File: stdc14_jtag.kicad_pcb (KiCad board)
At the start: 2 copper layers, 38 x 29 mm, 7 parts, among them J1 STDC14, J2 JTAG14, J3 UART, J4 POWER, SW1 RST

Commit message: fix: solve bottom silkscreen legend errors
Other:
- board text added: "CLK"
- board text added: "IO/MS"
- board text removed: "SWCLK/TCK"
- board text removed: "SWDIO/TMS"
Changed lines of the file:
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@@
       ) (layer "B.SilkS") (width 0.01) (fill solid))
   )
-  (gr_line (start -403 83.82) (end -403 87.376) (layer "B.SilkS") (width 0.15))
-  (gr_line (start -403 76.708) (end -403.75 76.708) (layer "B.SilkS") (width 0.15))
-  (gr_line (start -403 80.2) (end -403 76.708) (layer "B.SilkS") (width 0.15))
-  (gr_line (start -403 87.376) (end -403.75 87.376) (layer "B.SilkS") (width 0.15))
+  (gr_line (start -415.036 86.36) (end -415.036 82.042) (layer "B.SilkS") (width 0.15))
+  (gr_line (start -415.798 92.202) (end -414.274 92.202) (layer "B.SilkS") (width 0.15))
+  (gr_line (start -415.036 88.392) (end -415.036 92.202) (layer "B.SilkS") (width 0.15))
+  (gr_line (start -415.798 82.042) (end -414.274 82.042) (layer "B.SilkS") (width 0.15))
   (gr_line (start -402 95) (end -402 74) (layer "Edge.Cuts") (width 0.1))
   (gr_arc (start -436 99) (mid -438.828427 97.828427) (end -440 95) (layer "Edge.Cuts") (width 0.1))
@@
   (gr_line (start -406 70) (end -436 70) (layer "Edge.Cuts") (width 0.1))
   (gr_arc (start -402 95) (mid -403.171573 97.828427) (end -406 99) (layer "Edge.Cuts") (width 0.1))
-  (gr_text "GND" (at -403 82 90) (layer "B.SilkS")
+  (gr_text "GND" (at -415.036 87.376) (layer "B.SilkS")
+    (effects (font (size 1 1) (thickness 0.15)) (justify mirror))
+  )
+  (gr_text "RST" (at -415.036 79.502) (layer "B.SilkS")
     (effects (font (size 1 1) (thickness 0.15)) (justify mirror))
   )
@@
     (effects (font (size 1.5 1.5) (thickness 0.3)) (justify right mirror))
   )
-  (gr_text "SWCLK/TCK" (at -409 87.2) (layer "B.SilkS")
+  (gr_text "CLK" (at -409.448 82.042) (layer "B.SilkS")
     (effects (font (size 1 1) (thickness 0.15)) (justify left mirror))
   )
-  (gr_text "JTDI" (at -409 82.12) (layer "B.SilkS")
+  (gr_text "JTDI" (at -409.448 87.122) (layer "B.SilkS")
     (effects (font (size 1 1) (thickness 0.15)) (justify left mirror))
   )
@@
     (effects (font (size 1.5 1.5) (thickness 0.3)) (justify right mirror))
   )
-  (gr_text "VCC" (at -409 92.28) (layer "B.SilkS")
+  (gr_text "VCC" (at -409.448 76.962) (layer "B.SilkS")
     (effects (font (size 1 1) (thickness 0.15)) (justify left mirror))
   )
-  (gr_text "NC" (at -409 79.58) (layer "B.SilkS")
-    (effects (font (size 1 1) (thickness 0.15)) (justify left mirror))
-  )
-  (gr_text "RST" (at -403 89.25 90) (layer "B.SilkS")
-    (effects (font (size 1 1) (thickness 0.15)) (justify mirror))
+  (gr_text "NC" (at -411.734 89.662) (layer "B.SilkS")
+    (effects (font (size 1 1) (thickness 0.15)) (justify right mirror))
   )
   (gr_text "GND" (at -425.37 94 90) (layer "B.SilkS")
     (effects (font (size 1.5 1.5) (thickness 0.3)) (justify right mirror))
   )
-  (gr_text "SWDIO/TMS" (at -409 84.66) (layer "B.SilkS")
+  (gr_text "IO/MS" (at -409.448 84.582) (layer "B.SilkS")
     (effects (font (size 1 1) (thickness 0.15)) (justify left mirror))
   )
-  (gr_text "SWO" (at -409 89.74) (layer "B.SilkS")
+  (gr_text "SWO" (at -409.448 79.502) (layer "B.SilkS")
     (effects (font (size 1 1) (thickness 0.15)) (justify left mirror))
   )
-  (gr_text "GND" (at -403 92.75 90) (layer "B.SilkS")
-    (effects (font (size 1 1) (thickness 0.15)) (justify mirror))
-  )
-  (gr_text "NC" (at -409 77.04) (layer "B.SilkS")
-    (effects (font (size 1 1) (thickness 0.15)) (justify left mirror))
+  (gr_text "NC" (at -411.734 92.202) (layer "B.SilkS")
+    (effects (font (size 1 1) (thickness 0.15)) (justify right mirror))
   )
   (gr_text "STDC14 to JTAG 14\nAdapter" (at -435.75 84.5 90) (layer "B.SilkS")
     (effects (font (size 1.5 1.5) (thickness 0.3)) (justify mirror))
   )
+  (gr_text "GND" (at -415.036 76.962) (layer "B.SilkS")
+    (effects (font (size 1 1) (thickness 0.15)) (justify mirror))
+  )
   (gr_text "RST" (at -428 74.5 90) (layer "F.SilkS")

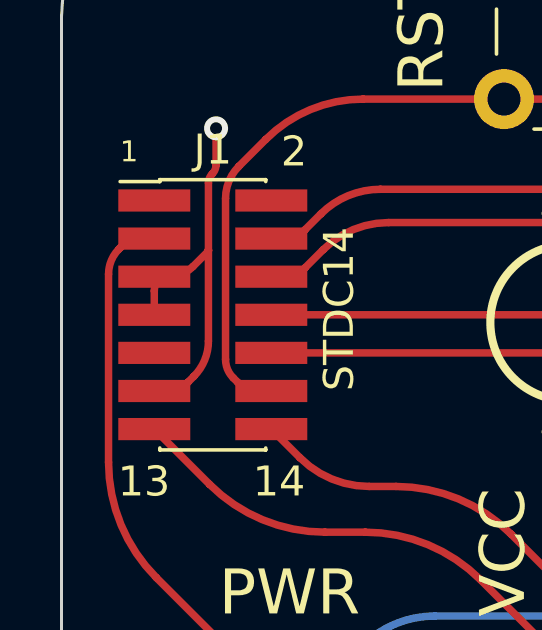
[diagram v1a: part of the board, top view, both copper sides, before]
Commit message: feat: replace OSHW symbol with Frullino
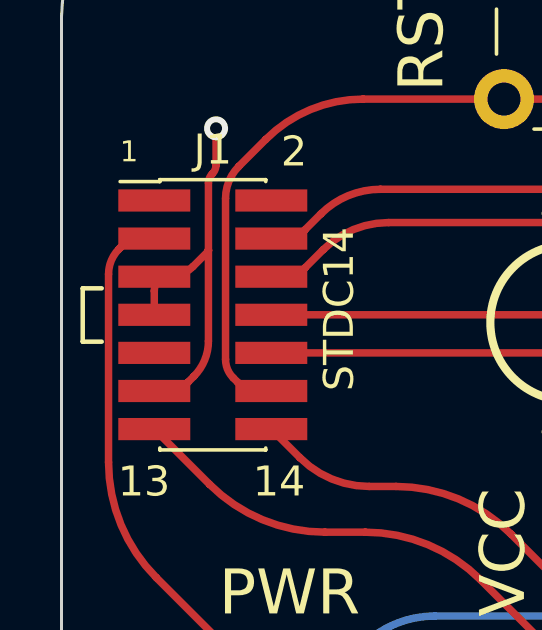
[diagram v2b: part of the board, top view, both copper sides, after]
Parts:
- removed REF**: OSHW-Symbol_6.7x6mm_SilkScreen, Symbol:OSHW-Symbol_6.7x6mm_SilkScreen
- added G***: LOGO, Symbols_Extra:Frullino-Logo_10x7, B.Cu at (-422.9, 83.9)
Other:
- board text added: "github.com/poggiolo"

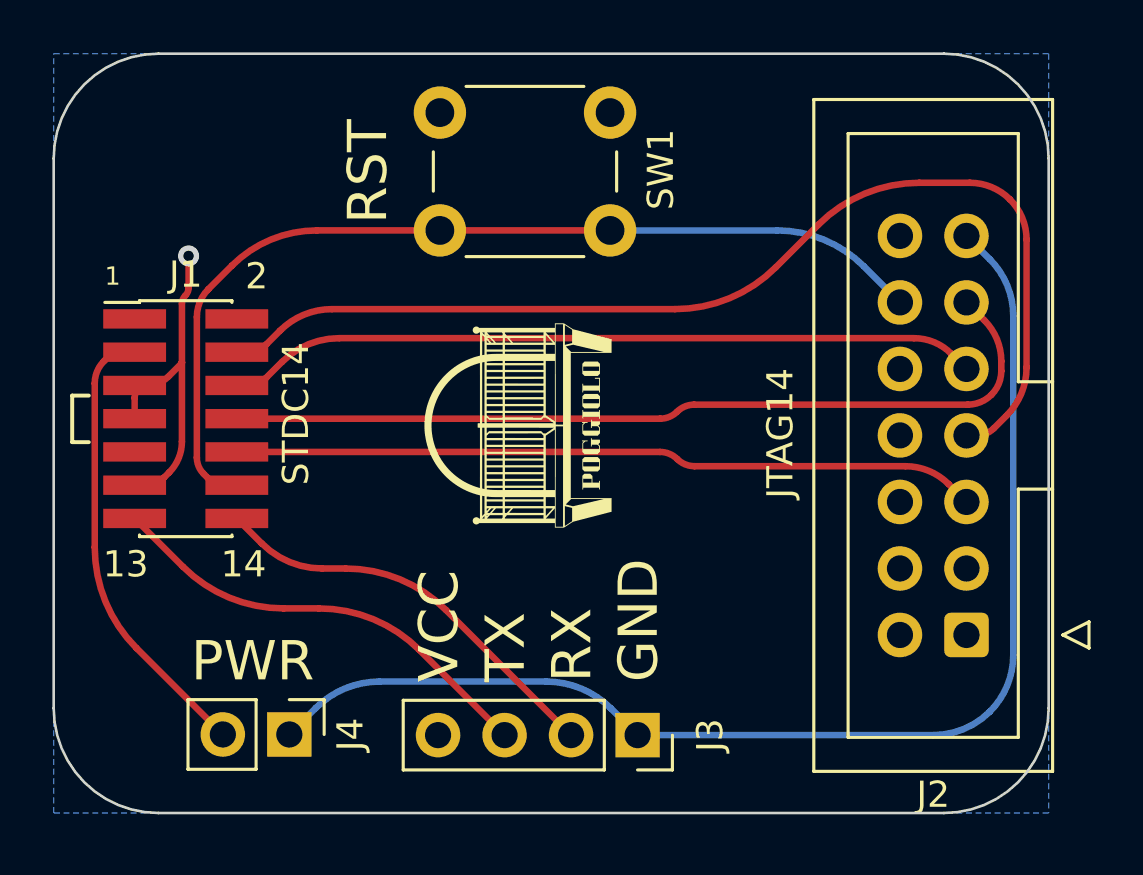
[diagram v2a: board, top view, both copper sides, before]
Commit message: chore: thicken power lines
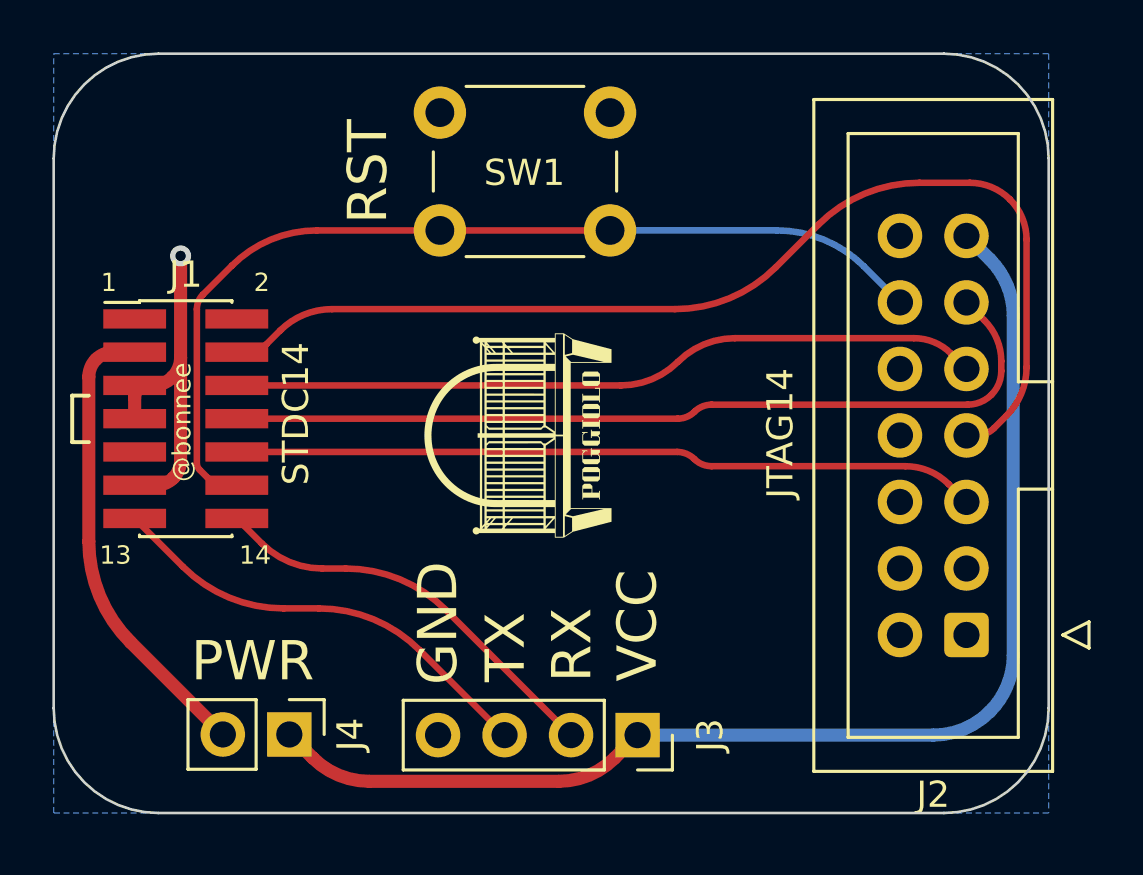
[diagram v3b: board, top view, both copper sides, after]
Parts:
- moved G*** 0.63 mm to (-422.9, 84.6)
- moved G*** 0.38 mm to (-422.4, 84.6)
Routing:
- net GND: track 13.1 -> 14.4 mm
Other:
- board text added: "@bonnee"

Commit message: feat: add front ground plane
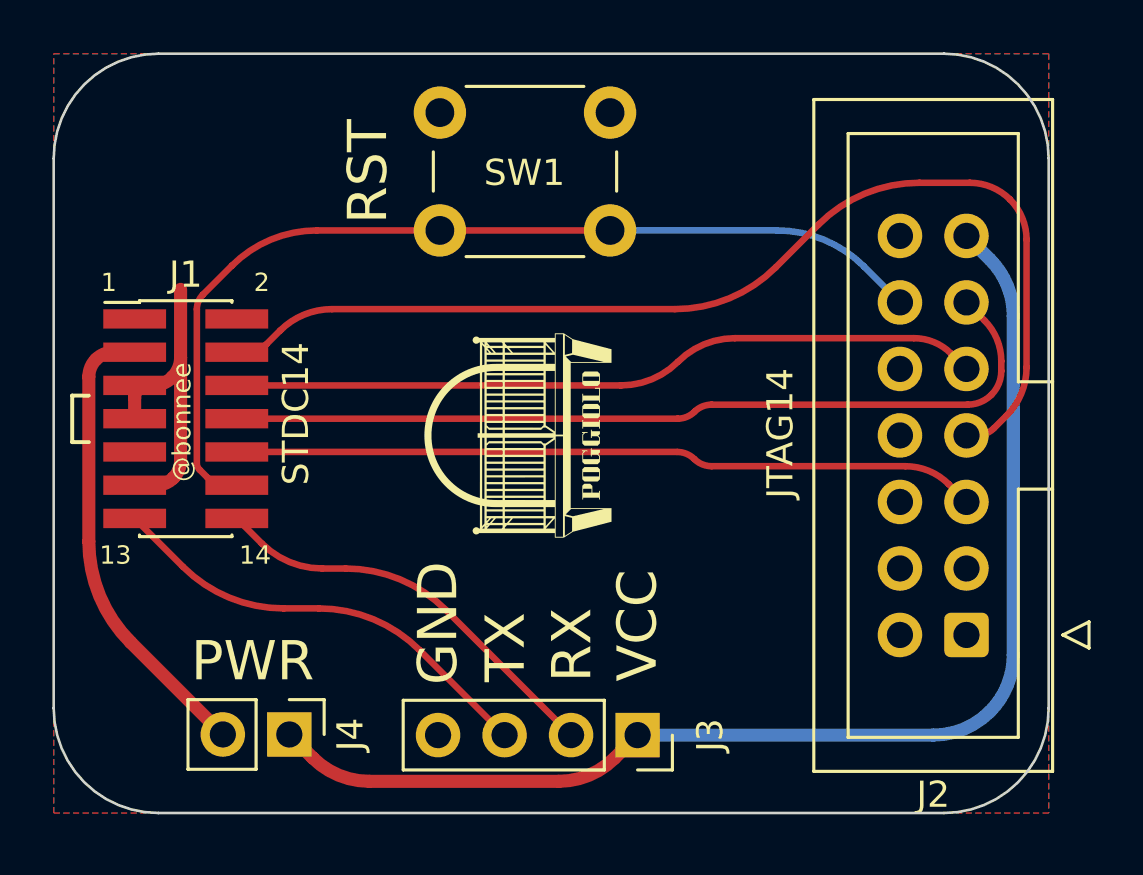
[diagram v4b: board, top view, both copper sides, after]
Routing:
- net GND: track 14.4 -> 13.1 mm, vias 1 -> 0
- added copper zone on F.Cu, net GND
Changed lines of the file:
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@@
   (segment (start -436.224863 82.67) (end -436.907 82.67) (width 0.5) (layer "F.Cu") (net 5))
   (segment (start -436.098878 86.48) (end -436.907 86.48) (width 0.5) (layer "F.Cu") (net 5))
+  (segment (start -435.1528 81.597936) (end -435.1528 79) (width 0.5) (layer "F.Cu") (net 5))
   (segment (start -436.907 83.145) (end -436.907 83.94) (width 0.5) (layer "F.Cu") (net 5))
   (segment (start -435.1528 82.486063) (end -435.1528 85.533921) (width 0.5) (layer "F.Cu") (net 5))
-  (segment (start -435.1528 81.597936) (end -435.1528 77.724) (width 0.5) (layer "F.Cu") (net 5))
-  (via (at -435.1528 77.724) (size 0.8) (drill 0.4) (layers "F.Cu" "B.Cu") (free) (net 5))
   (arc (start -436.907 83.145) (mid -436.767875 82.809124) (end -436.432 82.67) (width 0.5) (layer "F.Cu") (net 5))
   (arc (start -435.1528 82.486063) (mid -435.266347 82.316127) (end -435.4668 82.356) (width 0.5) (layer "F.Cu") (net 5))
@@
   (arc (start -425.014838 91.250161) (mid -426.773966 90.074749) (end -428.849 89.662) (width 0.25) (layer "F.Cu") (net 13))
   (arc (start -429.743011 89.662) (mid -430.992085 89.413543) (end -432.051 88.706) (width 0.25) (layer "F.Cu") (net 13))
+  (zone (net 5) (net_name "GND") (layer "F.Cu") (hatch edge 0.508)
+    (connect_pads (clearance 0.508))
+    (min_thickness 0.254) (filled_areas_thickness no)
+    (fill yes (thermal_gap 0.508) (thermal_bridge_width 0.508))
+    (polygon
+      (pts
+        (xy -402 99)
+        (xy -440 99)
+        (xy -440 70)
+        (xy -402 70)
+      )
+    )
+  )
   (zone (net 5) (net_name "GND") (layer "B.Cu") (name "GND") (hatch edge 0.508)
     (connect_pads (clearance 0.508))
